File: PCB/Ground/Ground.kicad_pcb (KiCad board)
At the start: 2 copper layers, 100 x 86.6 mm, 39 parts, among them CN1 GROVE, CN2 GROVE, CN3 GROVE, CN4 GROVE, CN5 GROVE, CN6 TTL-232R-3V3, CN7 ST-LINK, CN8 Conn_01x05_Female, CN9 CardEdgeConnector5P, SW1 RESET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

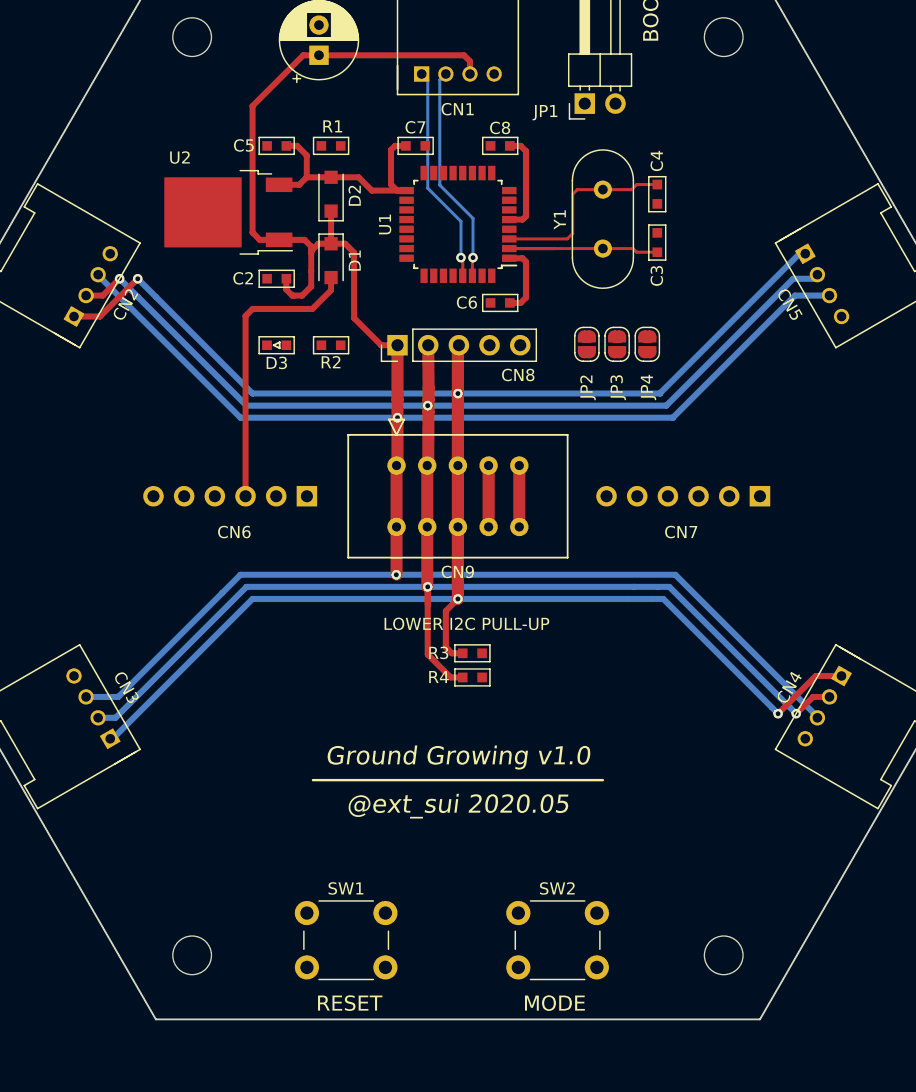
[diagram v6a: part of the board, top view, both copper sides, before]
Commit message: [update] Groundの回路図の細かい配線を一通り作成 #4
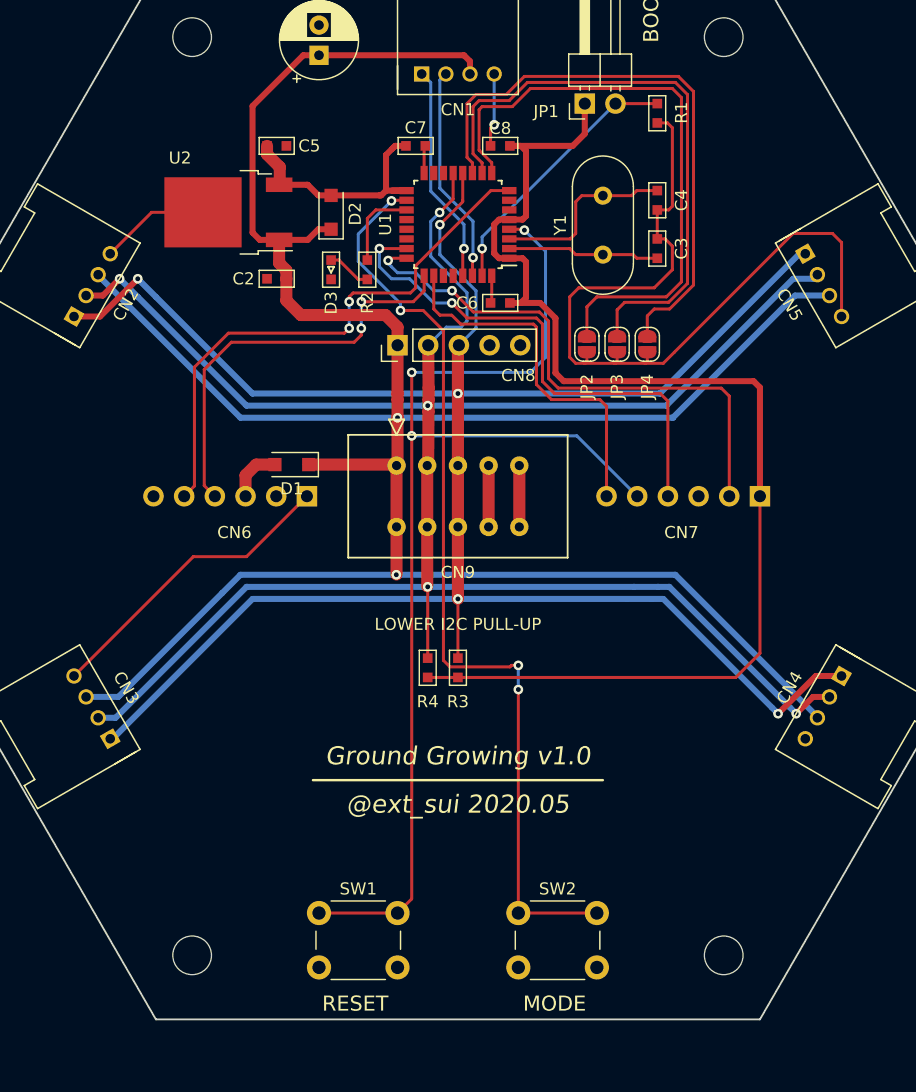
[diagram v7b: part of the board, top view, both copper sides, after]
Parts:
- moved R1 27.1 mm to (146.5, 73.3), turned to 270 degrees
- moved D1 17.2 mm to (116.2, 102.4), turned to 180 degrees
- moved SW1 8.75 mm to (125.0, 144.0), turned to 180 degrees
- moved D3 7.70 mm to (119.5, 86.2), turned to 90 degrees
- moved R2 6.93 mm to (122.5, 86.2), turned to 270 degrees
- moved R4 3.79 mm to (127.5, 119.2), turned to 90 degrees
- moved R3 1.70 mm to (130.0, 119.2), turned to 90 degrees
- moved D2 1.50 mm to (119.5, 81.5)
- moved C3 0.50 mm to (146.5, 84.5)
- moved C4 0.50 mm to (146.5, 80.5)
- moved Y1 0.50 mm to (142.0, 85.0)
- turned C5 to 0 degrees
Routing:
- net GND: track 5.19 -> 116.5 mm, vias 0 -> 1
- net NRST: track 0.00 -> 96.6 mm, vias 0 -> 3
- net 3V3: track 34.4 -> 125.2 mm
- net Net-(SW2-Pad1): track 0.00 -> 78.0 mm, vias 0 -> 4
- net Net-(JP2-Pad2): track 0.00 -> 49.9 mm
- net Net-(JP3-Pad2): track 0.00 -> 49.4 mm
- net Net-(JP4-Pad2): track 0.00 -> 48.7 mm
- net RXD: track 0.00 -> 45.7 mm, vias 0 -> 2
- net SWCLK: track 0.00 -> 45.7 mm, vias 0 -> 2
- net SWDIO: track 0.00 -> 42.9 mm, vias 0 -> 2
- net TXD: track 0.00 -> 34.6 mm, vias 0 -> 2
- net SWO: track 0.00 -> 30.6 mm
- net Net-(JP1-Pad2): track 0.00 -> 22.3 mm, vias 0 -> 1
- net Net-(CN6-Pad3): track 23.9 -> 4.53 mm
- net LOWER_SCL: track 168.7 -> 184.5 mm, vias 4 -> 5
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
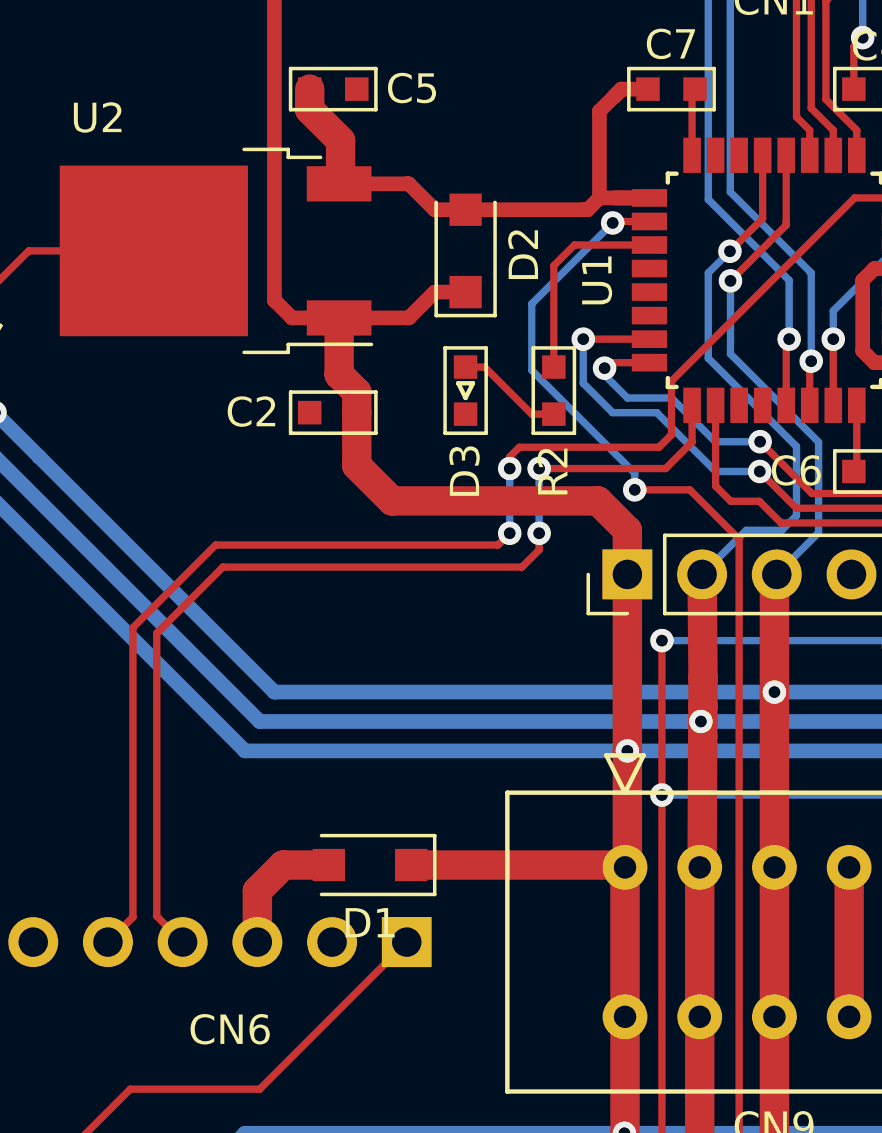
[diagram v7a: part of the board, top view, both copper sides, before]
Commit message: [update] GroundのD1,D2のフットプリントを変更 #4
* 実物合わせの結果123Fより123の方が適合していた
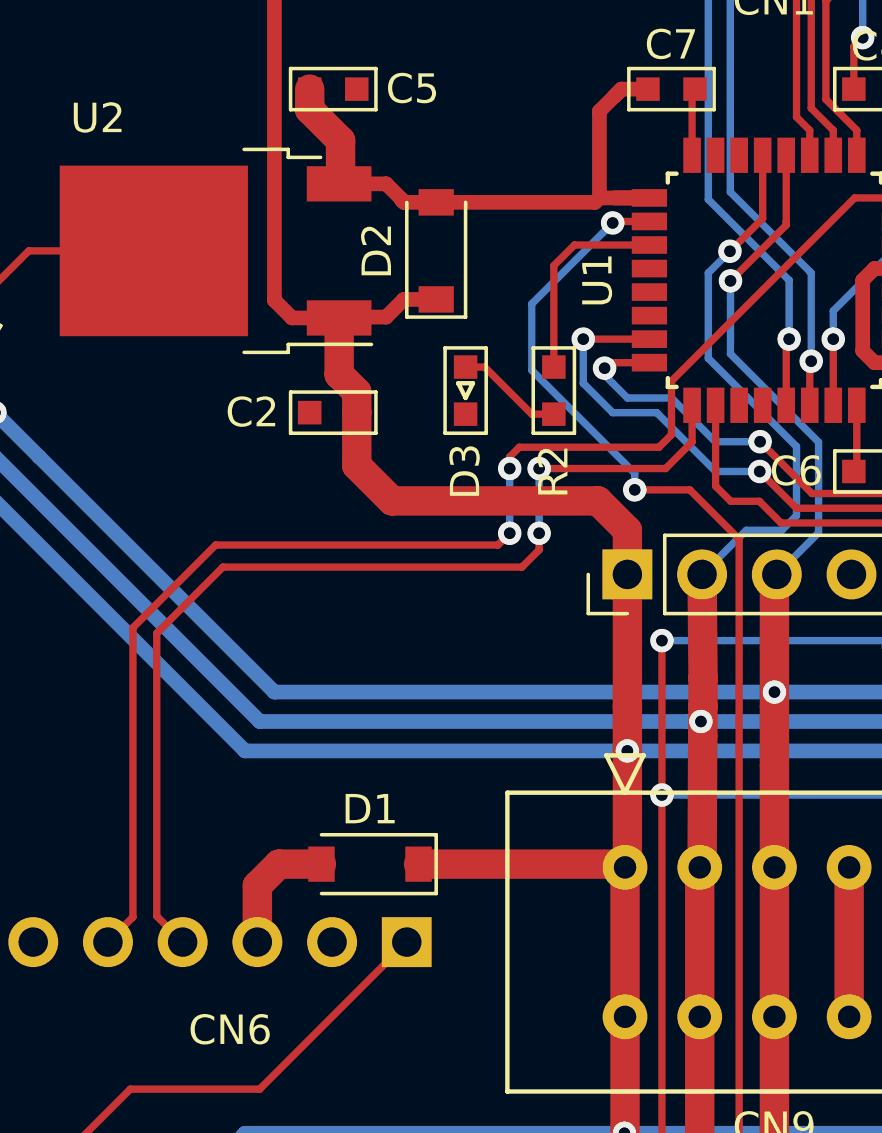
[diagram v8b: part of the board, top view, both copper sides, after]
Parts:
- D1, D2: footprint Diode_SMD:D_SOD-123F -> Diode_SMD:D_SOD-123
- moved D2 1.00 mm to (118.5, 81.5)
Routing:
- net 5V: track 221.7 -> 220.4 mm
